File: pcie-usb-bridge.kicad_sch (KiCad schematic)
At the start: 50 parts, among them IC1 UPD720201K8-711-BAC-A, U2 SST25VF512A, Y1 NX3225SA-24M

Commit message: Loclib
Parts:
- IC1: footprint antmicro-footprints:QFN40P800X800X90-69N-D -> m2-smart-iot-module-footprints:QFN40P800X800X90-69N-D; symbol antmicroInterfaceControllers:UPD720201K8-711-BAC-A -> m2-smart-iot-module:UPD720201K8-711-BAC-A
- R47, R48: footprint antmicro-footprints:0402-res -> m2-smart-iot-module-footprints:0402-res
- R49, R50, R51, R52: footprint antmicro-footprints:0402-res -> m2-smart-iot-module-footprints:0402-res; symbol antmicroResistors0402:R_0R_0402 -> m2-smart-iot-module:R_0R_0402

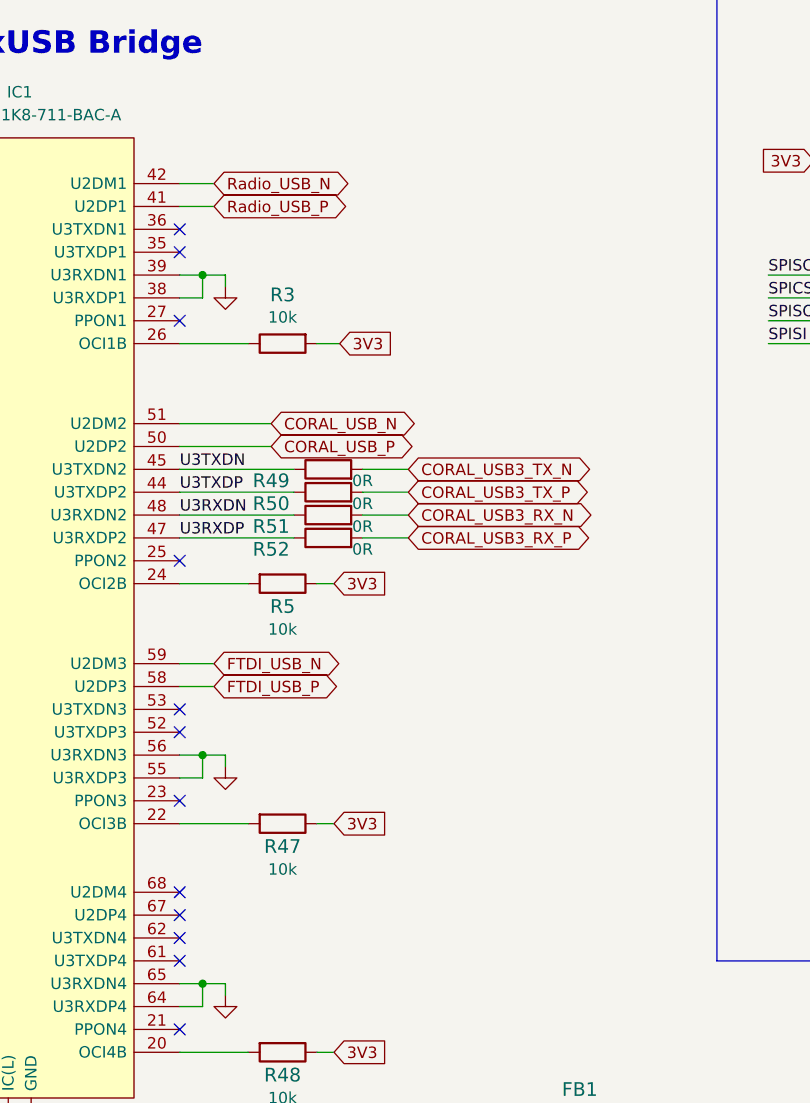
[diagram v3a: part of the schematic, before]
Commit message: Add OR resistors to outputs of the PCIE-USB bridge and FTDI
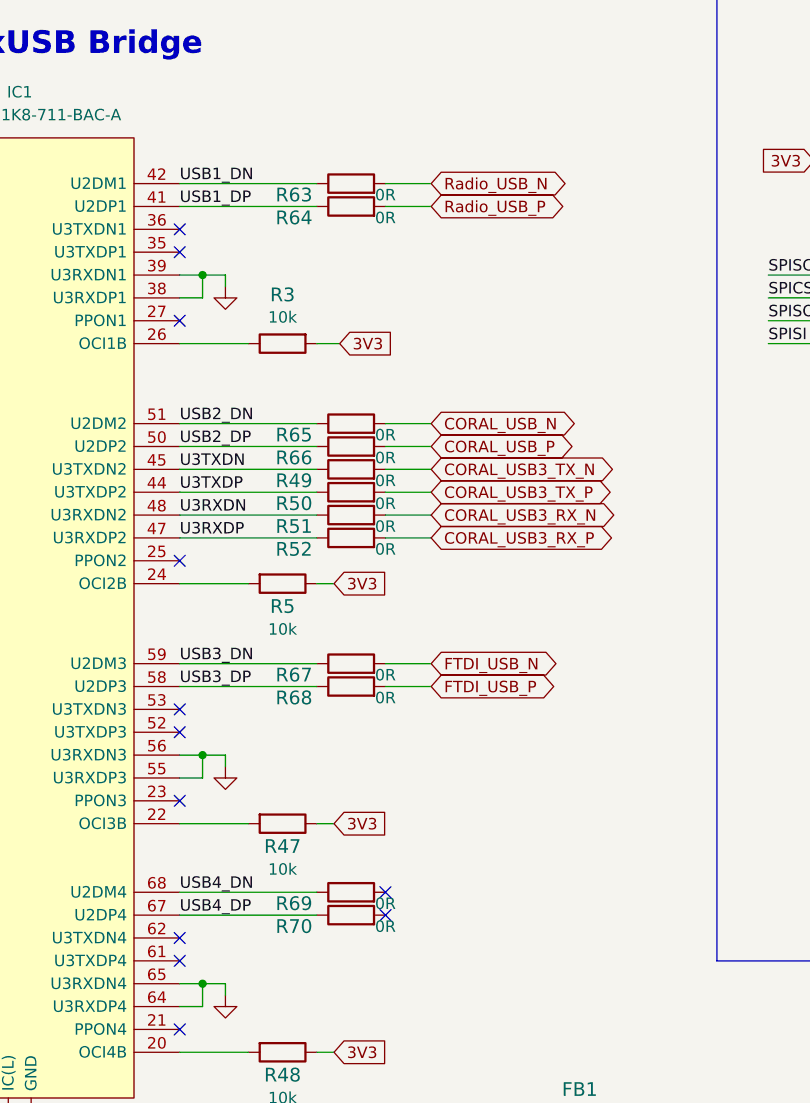
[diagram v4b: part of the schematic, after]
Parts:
- added R63, R64, R65, R66, R67, R68, R69, R70: R_0R_0402, m2-smart-iot-module-footprints:0402-res, symbol m2-smart-iot-module:R_0R_0402
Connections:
- net CORAL_USB_N: now also R65.2; no longer IC1.51 (U2DM2)
- net CORAL_USB_P: now also R66.2; no longer IC1.50 (U2DP2)
- net FTDI_USB_N: now also R67.2; no longer IC1.59 (U2DM3)
- net FTDI_USB_P: now also R68.2; no longer IC1.58 (U2DP3)
- net Radio_USB_N: now also R63.2; no longer IC1.42 (U2DM1)
- net Radio_USB_P: now also R64.2; no longer IC1.41 (U2DP1)
- net USB4_DP: now reaches IC1.67 (U2DP4)
- net USB4_DP: now also R70.1
- net USB4_DN: now reaches IC1.68 (U2DM4)
- net USB4_DN: now also R69.1
- new net USB1_DN: IC1.42 (U2DM1), R63.1
- new net USB1_DP: IC1.41 (U2DP1), R64.1
- new net USB2_DN: IC1.51 (U2DM2), R65.1
- new net USB2_DP: IC1.50 (U2DP2), R66.1
- new net USB3_DN: IC1.59 (U2DM3), R67.1
- new net USB3_DP: IC1.58 (U2DP3), R68.1
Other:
- moved on the sheet: R49, R50, R51, R52
